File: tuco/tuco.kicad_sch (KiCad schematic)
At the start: 5 parts, among them J1 Conn_02x10_Odd_Even, J2 Conn_02x10_Odd_Even, J3 TSM-108-01-F-DV, J4 S16B-XH-A, U1 Teensy4.1

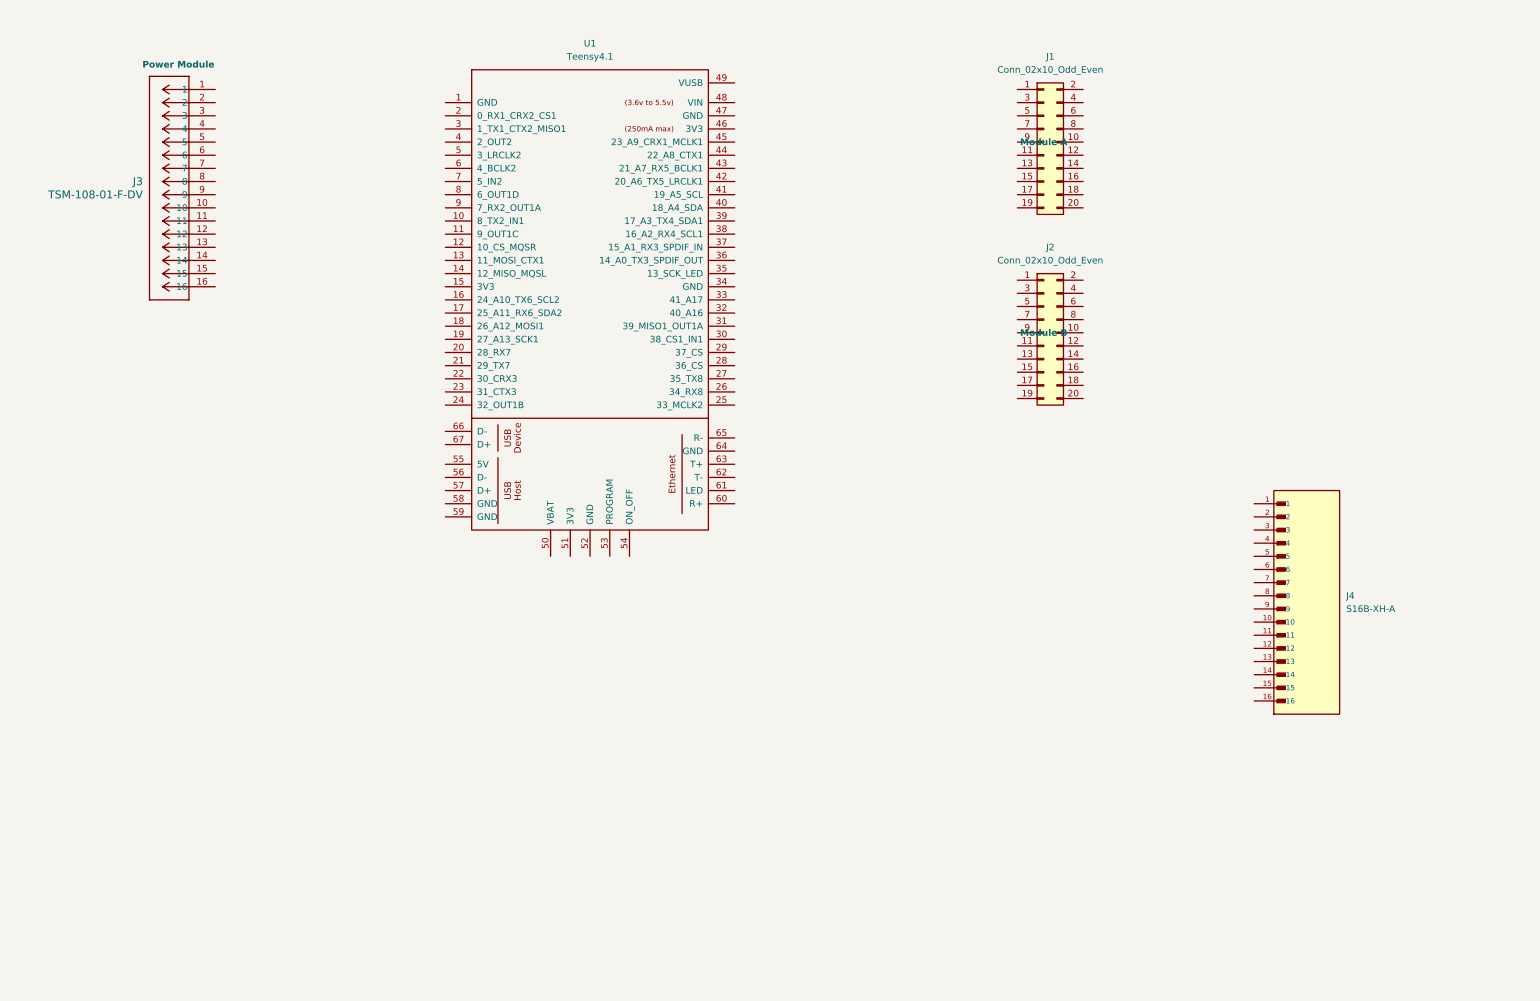
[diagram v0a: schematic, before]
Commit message: Created Tuco board outline, heisenberg pin labels
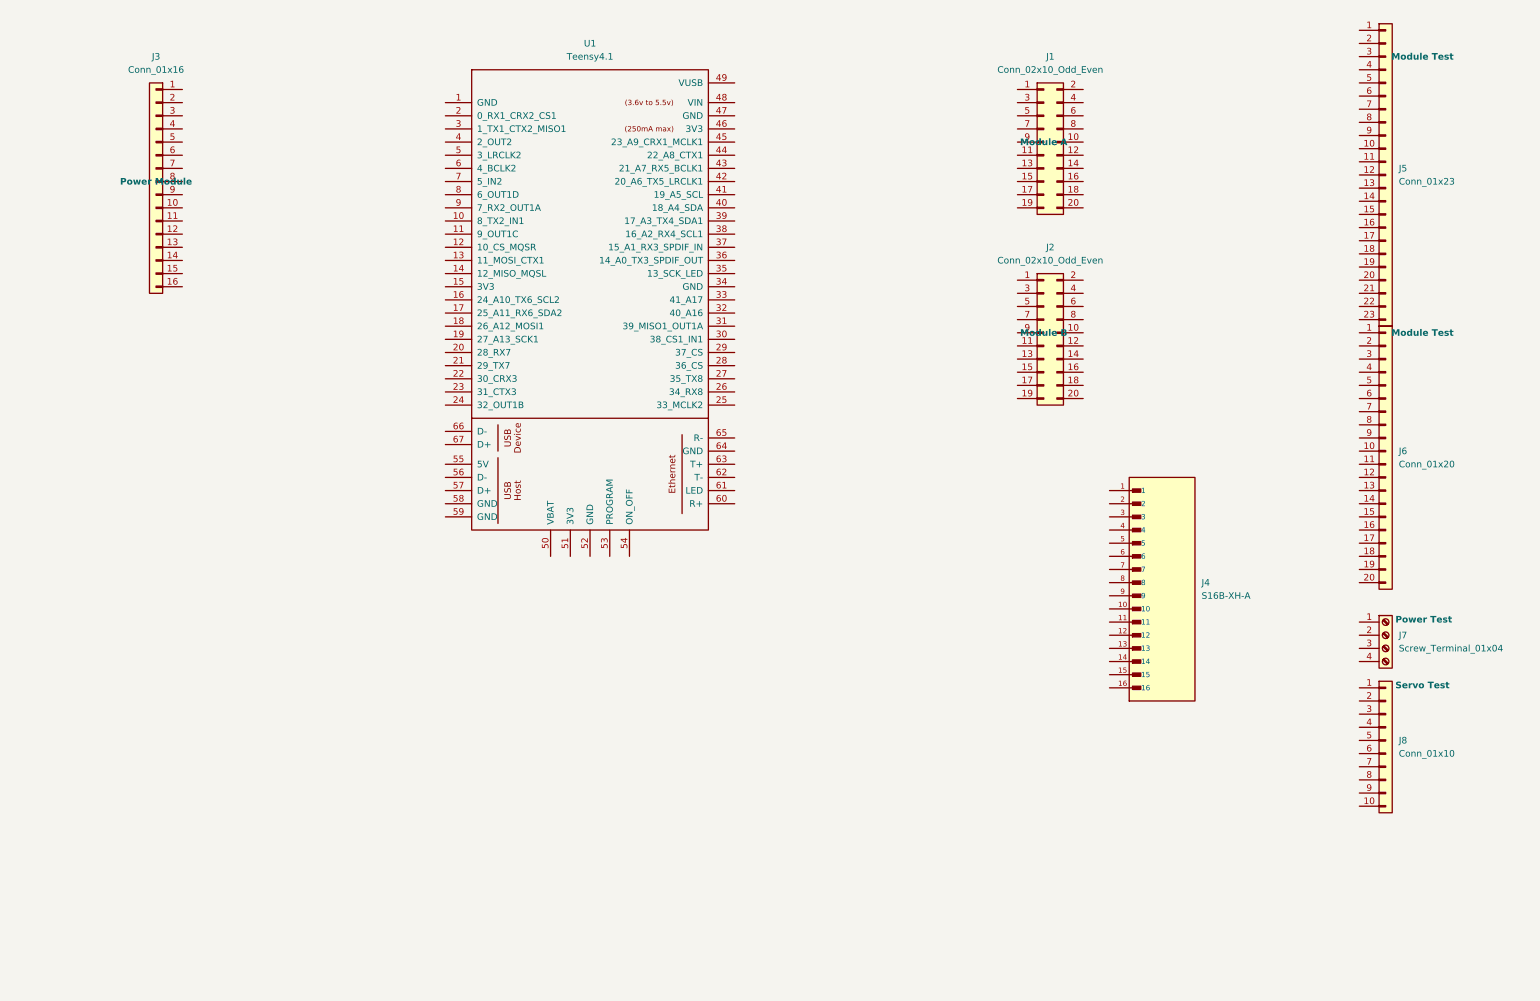
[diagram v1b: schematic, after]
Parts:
- removed J3: TSM-108-01-F-DV, MDFC Common:CONN_TSM-108-01-F-DV_SAI, symbol MDFC Common:TSM-108-01-F-DV
- added J3: Conn_01x16, PinHeader_2x08_P2.54mm_Vertical, symbol Connector_Generic:Conn_01x16
- added J5: Conn_01x23, PinHeader_1x23_P2.54mm_Vertical, symbol Connector_Generic:Conn_01x23
- added J6: Conn_01x20, PinHeader_1x20_P2.54mm_Vertical, symbol Connector_Generic:Conn_01x20
- added J7: Screw_Terminal_01x04, TerminalBlock_Phoenix_PT-1,5-4-5.0-H_1x04_P5.00mm_Horizontal, symbol Connector:Screw_Terminal_01x04
- added J8: Conn_01x10, PinHeader_1x10_P2.54mm_Vertical, symbol Connector_Generic:Conn_01x10
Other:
- moved on the sheet: J4

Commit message: TUCO: Added net labels, servo/power prelim pinouts
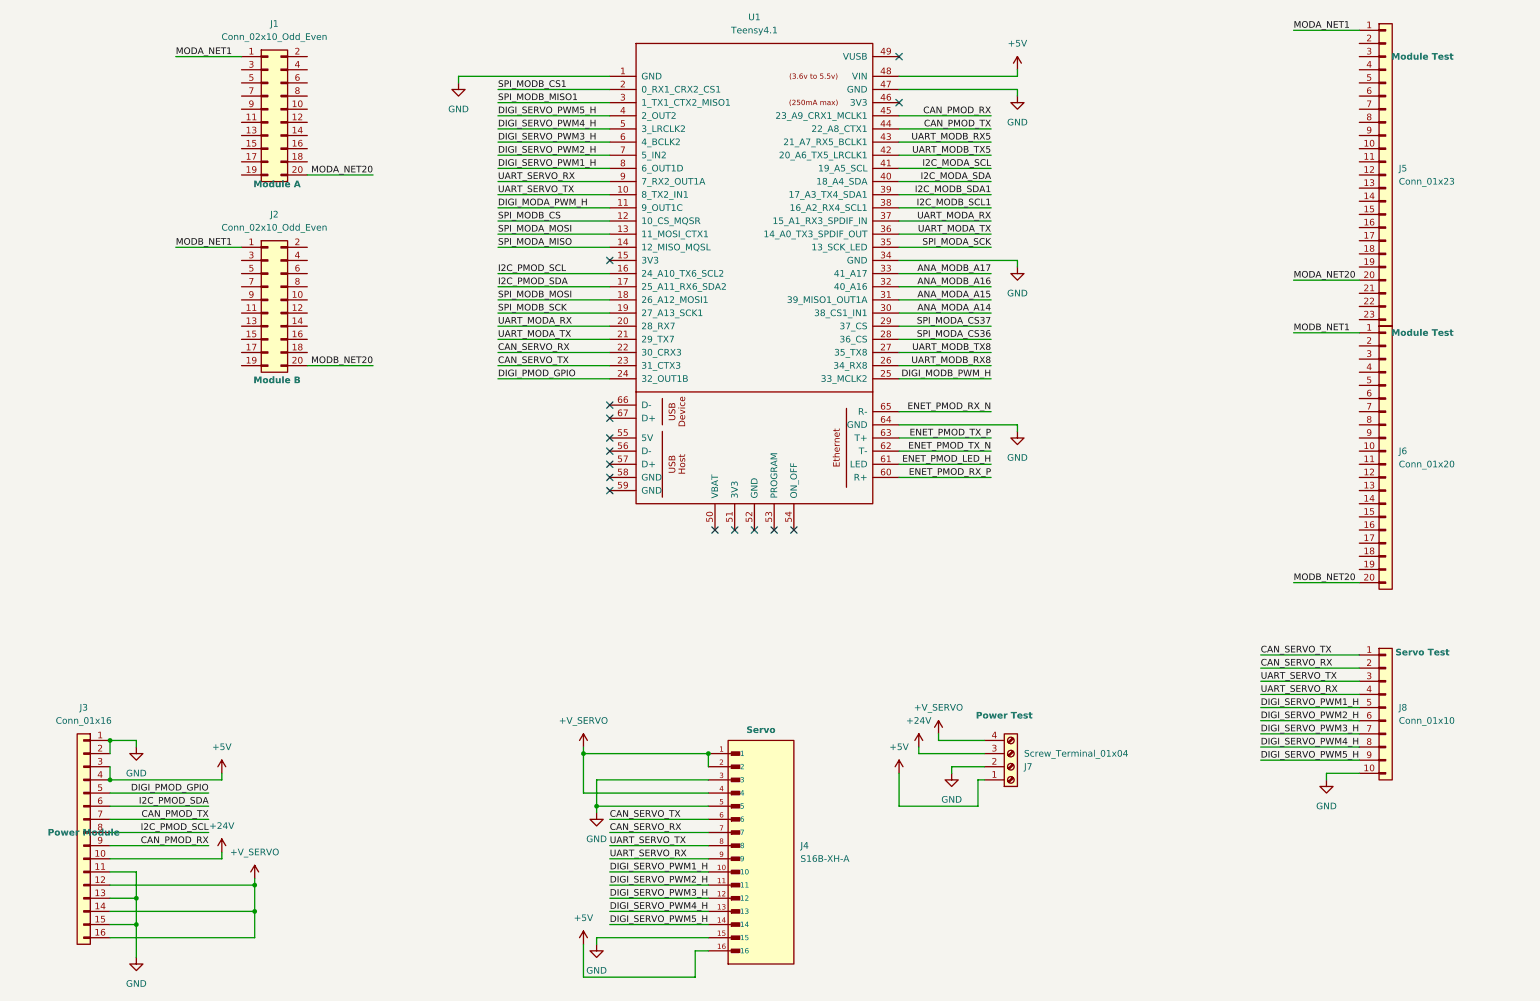
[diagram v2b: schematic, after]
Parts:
- J4: Label (none) -> Servo
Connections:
- net MODB_NET1: now reaches J6.1 (Pin_1)
- net MODB_NET1: now also J2.1 (Pin_1)
- net MODB_NET20: now reaches J6.20 (Pin_20)
- net MODB_NET20: now also J2.20 (Pin_20)
- net MODA_NET1: now reaches J1.1 (Pin_1)
- net MODA_NET1: now also J5.1 (Pin_1)
- net MODA_NET20: now reaches J1.20 (Pin_20)
- net MODA_NET20: now also J5.20 (Pin_20)
- net GND: now reaches J3.1 (Pin_1)
- net GND: now also J3.11 (Pin_11), J3.13 (Pin_13), J3.15 (Pin_15), J3.2 (Pin_2), J4.15, J4.3, J4.5, J7.2 (Pin_2), J8.10 (Pin_10), U1.1 (GND), U1.34 (GND), U1.47 (GND), U1.64 (GND)
- net +24V: now reaches J3.10 (Pin_10)
- net +24V: now also J7.3 (Pin_3)
- net +V_SERVO: now reaches J3.12 (Pin_12)
- net +V_SERVO: now also J3.14 (Pin_14), J3.16 (Pin_16), J4.1, J4.2, J4.4, J7.4 (Pin_4)
- net +5V: now reaches J3.3 (Pin_3)
- net +5V: now also J3.4 (Pin_4), J4.16, J7.1 (Pin_1), U1.48 (VIN)
- net DIGI_PMOD_GPIO: now reaches J3.5 (Pin_5)
- net DIGI_PMOD_GPIO: now also U1.24 (32_OUT1B)
- net I2C_PMOD_SDA: now reaches J3.6 (Pin_6)
- net I2C_PMOD_SDA: now also U1.17 (25_A11_RX6_SDA2)
- net CAN_PMOD_TX: now reaches J3.7 (Pin_7)
- net CAN_PMOD_TX: now also U1.44 (22_A8_CTX1)
- net I2C_PMOD_SCL: now reaches J3.8 (Pin_8)
- net I2C_PMOD_SCL: now also U1.16 (24_A10_TX6_SCL2)
- net CAN_PMOD_RX: now reaches J3.9 (Pin_9)
- net CAN_PMOD_RX: now also U1.45 (23_A9_CRX1_MCLK1)
- net DIGI_SERVO_PWM1_H: now reaches J4.10
- net DIGI_SERVO_PWM1_H: now also J8.5 (Pin_5), U1.8 (6_OUT1D)
- net DIGI_SERVO_PWM2_H: now reaches J4.11
- net DIGI_SERVO_PWM2_H: now also J8.6 (Pin_6), U1.7 (5_IN2)
- net DIGI_SERVO_PWM3_H: now reaches J4.12
- net DIGI_SERVO_PWM3_H: now also J8.7 (Pin_7), U1.6 (4_BCLK2)
- net DIGI_SERVO_PWM4_H: now reaches J4.13
- net DIGI_SERVO_PWM4_H: now also J8.8 (Pin_8), U1.5 (3_LRCLK2)
- net DIGI_SERVO_PWM5_H: now reaches J4.14
- net DIGI_SERVO_PWM5_H: now also J8.9 (Pin_9), U1.4 (2_OUT2)
- net CAN_SERVO_TX: now reaches J4.6
- net CAN_SERVO_TX: now also J8.1 (Pin_1), U1.23 (31_CTX3)
- net CAN_SERVO_RX: now reaches J4.7
- net CAN_SERVO_RX: now also J8.2 (Pin_2), U1.22 (30_CRX3)
- net UART_SERVO_TX: now reaches J4.8
- net UART_SERVO_TX: now also J8.3 (Pin_3), U1.10 (8_TX2_IN1)
- net UART_SERVO_RX: now reaches J4.9
- net UART_SERVO_RX: now also J8.4 (Pin_4), U1.9 (7_RX2_OUT1A)
- net DIGI_MODA_PWM_H: now reaches U1.11 (9_OUT1C)
- net SPI_MODB_CS: now reaches U1.12 (10_CS_MQSR)
- net SPI_MODA_MOSI: now reaches U1.13 (11_MOSI_CTX1)
- net SPI_MODA_MISO: now reaches U1.14 (12_MISO_MQSL)
- net SPI_MODB_MOSI: now reaches U1.18 (26_A12_MOSI1)
- net SPI_MODB_SCK: now reaches U1.19 (27_A13_SCK1)
- net SPI_MODB_CS1: now reaches U1.2 (0_RX1_CRX2_CS1)
- net UART_MODA_RX: now reaches U1.20 (28_RX7)
- net UART_MODA_RX: now also U1.37 (15_A1_RX3_SPDIF_IN)
- net UART_MODA_TX: now reaches U1.21 (29_TX7)
- net UART_MODA_TX: now also U1.36 (14_A0_TX3_SPDIF_OUT)
- net DIGI_MODB_PWM_H: now reaches U1.25 (33_MCLK2)
- net UART_MODB_RX8: now reaches U1.26 (34_RX8)
- net UART_MODB_TX8: now reaches U1.27 (35_TX8)
- net SPI_MODA_CS36: now reaches U1.28 (36_CS)
- net SPI_MODA_CS37: now reaches U1.29 (37_CS)
- net SPI_MODB_MISO1: now reaches U1.3 (1_TX1_CTX2_MISO1)
- net ANA_MODA_A14: now reaches U1.30 (38_CS1_IN1)
- net ANA_MODA_A15: now reaches U1.31 (39_MISO1_OUT1A)
- net ANA_MODB_A16: now reaches U1.32 (40_A16)
- net ANA_MODB_A17: now reaches U1.33 (41_A17)
- net SPI_MODA_SCK: now reaches U1.35 (13_SCK_LED)
- net I2C_MODB_SCL1: now reaches U1.38 (16_A2_RX4_SCL1)
- net I2C_MODB_SDA1: now reaches U1.39 (17_A3_TX4_SDA1)
- net I2C_MODA_SDA: now reaches U1.40 (18_A4_SDA)
- net I2C_MODA_SCL: now reaches U1.41 (19_A5_SCL)
- net UART_MODB_TX5: now reaches U1.42 (20_A6_TX5_LRCLK1)
- net UART_MODB_RX5: now reaches U1.43 (21_A7_RX5_BCLK1)
- net ENET_PMOD_RX_P: now reaches U1.60 (R+)
- net ENET_PMOD_LED_H: now reaches U1.61 (LED)
- net ENET_PMOD_TX_N: now reaches U1.62 (T-)
- net ENET_PMOD_TX_P: now reaches U1.63 (T+)
- net ENET_PMOD_RX_N: now reaches U1.65 (R-)
- no-connect marks 0 -> 15
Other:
- moved on the sheet: J1, J2, J3, J4, J7, J8, U1
